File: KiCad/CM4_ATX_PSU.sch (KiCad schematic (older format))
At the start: 2 parts, among them J7 39-28-1243, U2 AP7363-33D

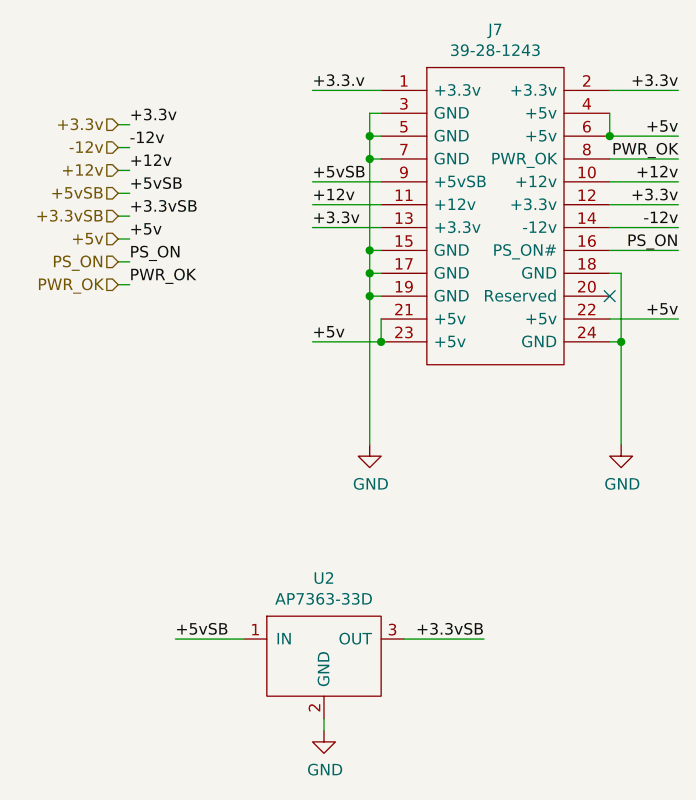
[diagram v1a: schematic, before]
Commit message: Added buffering caps to U2 (3.3vSB provider)
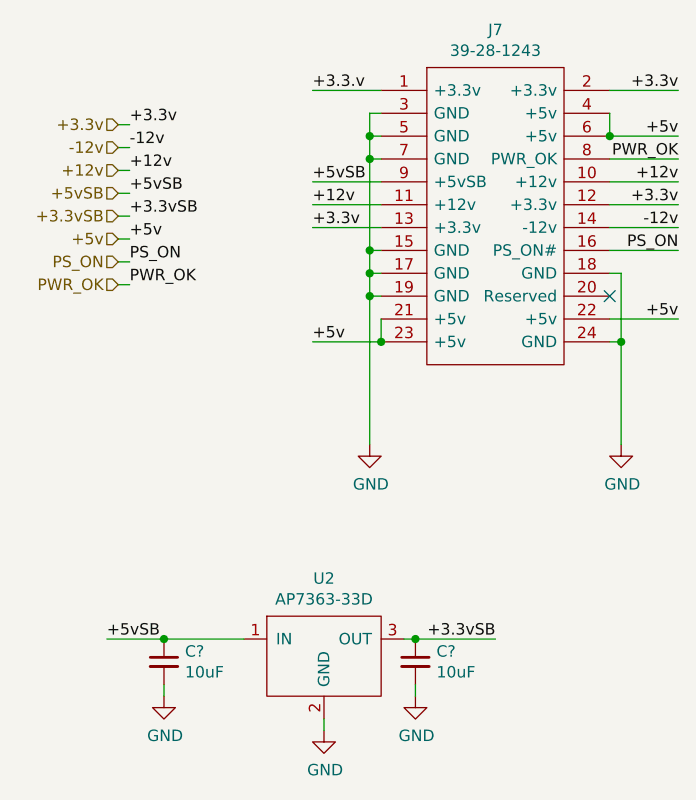
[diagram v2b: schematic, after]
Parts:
- added C? (x2): 10uF, symbol CM4_MATX:C_Small
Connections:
- net +3.3vSB: now also C?.1
- net +5vSB: now also C?.1
- net GND: now also C?.2, C?.2
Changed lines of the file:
@@
 Wire Wire Line
 	4800 4300 4850 4300
-Text Label 5050 5950 0    50   ~ 0
+Text Label 4750 5950 0    50   ~ 0
 +5vSB
 $Comp
@@
 	1    0    0    -1
 $EndComp
-Text Label 6400 5950 2    50   ~ 0
+Text Label 6450 5950 2    50   ~ 0
 +3.3vSB
 Wire Wire Line
-	5050 5950 5350 5950
+	4750 5950 5000 5950
 Wire Wire Line
-	6050 5950 6400 5950
+	6100 5950 6450 5950
 $Comp
 L CM4_MATX:GND #PWR0209
@@
 Wire Wire Line
 	4800 4100 4850 4100
+$Comp
+L CM4_MATX:C_Small C?
+U 1 1 602F3F91
+P 5000 6050
+F 0 "C?" H 5092 6096 50  0000 L CNN
+F 1 "10uF" H 5092 6005 50  0000 L CNN
+F 2 "" H 5000 6050 50  0001 C CNN
+F 3 "~" H 5000 6050 50  0001 C CNN
+	1    5000 6050
+	1    0    0    -1
+$EndComp
+Connection ~ 5000 5950
+Wire Wire Line
+	5000 5950 5350 5950
+$Comp
+L CM4_MATX:GND #PWR?
+U 1 1 602F5A61
+P 5000 6200
+F 0 "#PWR?" H 5000 5950 50  0001 C CNN
+F 1 "GND" H 5005 6027 50  0000 C CNN
+F 2 "" H 5000 6200 50  0001 C CNN
+F 3 "" H 5000 6200 50  0001 C CNN
+	1    5000 6200
+	1    0    0    -1
+$EndComp
+Wire Wire Line
+	5000 6200 5000 6150
+$Comp
+L CM4_MATX:C_Small C?
+U 1 1 602F74E7
+P 6100 6050
+F 0 "C?" H 6192 6096 50  0000 L CNN
+F 1 "10uF" H 6192 6005 50  0000 L CNN
+F 2 "" H 6100 6050 50  0001 C CNN
+F 3 "~" H 6100 6050 50  0001 C CNN
+	1    6100 6050
+	1    0    0    -1
+$EndComp
+Wire Wire Line
+	6100 5950 6050 5950
+Connection ~ 6100 5950
+$Comp
+L CM4_MATX:GND #PWR?
+U 1 1 602F8449
+P 6100 6200
+F 0 "#PWR?" H 6100 5950 50  0001 C CNN
+F 1 "GND" H 6105 6027 50  0000 C CNN
+F 2 "" H 6100 6200 50  0001 C CNN
+F 3 "" H 6100 6200 50  0001 C CNN
+	1    6100 6200
+	1    0    0    -1
+$EndComp
+Wire Wire Line
+	6100 6200 6100 6150
 $EndSCHEMATC

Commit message: Started picking passive components, overhauled library
Cleaned up a bunch of schematic library references.
Added datasheets, descriptions for a lot of existing parts.
Picked most capacitor parts, still a couple left.
Cleaned up a fair few footprint references.
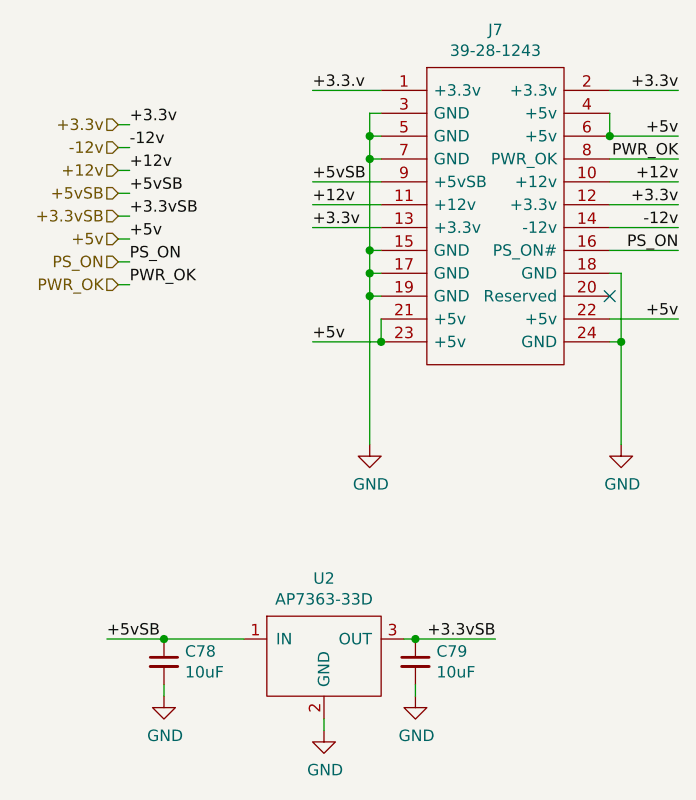
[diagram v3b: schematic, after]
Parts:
- C78, C79: renamed from C?; footprint (none) -> CM4_MATX:C_0603_1608Metric_Pad1.08x0.95mm_HandSolder; Description (none) -> 6.3V 10uF X5R 0603 20% Tol; Mfr. (none) -> Samsung; Mfr. No (none) -> CL10A106MQ8NNNC; Mouser Part Number (none) -> 187-CL10A106MQ8NNNC; Mouser Price/Stock (none) -> https://www.mouser.co.uk/ProductDetail/Samsung-Electro-Mech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
- J7: Height 13.1 -> (none); Manufacturer_Name Molex -> (none); Manufacturer_Part_Number 39-28-1243 -> (none); Mfr. (none) -> Molex; Mfr. No (none) -> 39-28-1243
- U2: footprint (none) -> CM4_MATX:TO-252-3_TabPin2; Description (none) -> LDO Voltage Regulators 1.5A Fast Transient Ultra-LDO Linear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; Mfr. (none) -> Diodes Inc.; Mfr. No (none) -> AP7363-33D-13; Mouser Part Number (none) -> 621-AP7363-33D-13; Mouser Price/Stock (none) -> https://www.mouser.co.uk/ProductDetail/Diodes-Incorporated/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
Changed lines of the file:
@@
 F 1 "39-28-1243" H 6450 3724 50  0000 C CNN
 F 2 "CM4_MATX:SHDR24W125P550X420_2X12_5160X960X1310P" H 6000 4500 50  0001 L CNN
-F 3 "" H 6700 3550 50  0001 L CNN
+F 3 "https://www.mouser.co.uk/datasheet/2/276/0039281243_PCB_HEADERS-228405.pdf" H 6700 3550 50  0001 L CNN
 F 4 "24 way vertical PCB header,Mini-Fit Jr Molex MINI-FIT JR. Series, Series Number 5566, 4.2mm Pitch 24 Way 2 Row Straight PCB Header, Solder Termination, 6A" H 6000 4300 50  0001 L CNN "Description"
-F 5 "13.1" H 6000 4200 50  0001 L CNN "Height"
-F 6 "538-39-28-1243" H 6000 4100 50  0001 L CNN "Mouser Part Number"
-F 7 "https://www.mouser.co.uk/ProductDetail/Molex/39-28-1243?qs=4XSMV6Twtb0I%2F4%252BTTSJFbg%3D%3D" H 6000 4000 50  0001 L CNN "Mouser Price/Stock"
-F 8 "Molex" H 6000 3900 50  0001 L CNN "Manufacturer_Name"
-F 9 "39-28-1243" H 6000 3800 50  0001 L CNN "Manufacturer_Part_Number"
+F 5 "538-39-28-1243" H 6000 4100 50  0001 L CNN "Mouser Part Number"
+F 6 "https://www.mouser.co.uk/ProductDetail/Molex/39-28-1243?qs=4XSMV6Twtb0I%2F4%252BTTSJFbg%3D%3D" H 6000 4000 50  0001 L CNN "Mouser Price/Stock"
+F 7 "Molex" H 5950 3550 50  0001 C CNN "Mfr."
+F 8 "39-28-1243" H 5950 3550 50  0001 C CNN "Mfr. No"
 	1    5950 3550
 	1    0    0    -1
@@
 	5900 3750 5900 3850
 $Comp
-L power:GND #PWR0109
+L CM4_MATX:GND #PWR0109
 U 1 1 601F254C
 P 5900 5100
@@
 	5900 4450 5900 5100
 $Comp
-L power:GND #PWR0110
+L CM4_MATX:GND #PWR0110
 U 1 1 5FF31AD9
 P 7000 5100
@@
 F 0 "U2" H 5700 6215 50  0000 C CNN
 F 1 "AP7363-33D" H 5700 6124 50  0000 C CNN
-F 2 "" H 5700 5950 50  0001 C CNN
+F 2 "CM4_MATX:TO-252-3_TabPin2" H 5700 5950 50  0001 C CNN
 F 3 "https://www.mouser.co.uk/datasheet/2/115/AP7363-247326.pdf" H 5700 5950 50  0001 C CNN
+F 4 "Diodes Inc." H 5700 5950 50  0001 C CNN "Mfr."
+F 5 "AP7363-33D-13" H 5700 5950 50  0001 C CNN "Mfr. No"
+F 6 "621-AP7363-33D-13" H 5700 5950 50  0001 C CNN "Mouser Part Number"
+F 7 "https://www.mouser.co.uk/ProductDetail/Diodes-Incorporated/AP7363-33D-13/?qs=%2Fha2pyFadugx5jr4Zj5yqo2rf4G2BFwG0SXqAhZYbUZbnjJLR6QP1A%3D%3D" H 5700 5950 50  0001 C CNN "Mouser Price/Stock"
+F 8 "LDO Voltage Regulators 1.5A Fast Transient Ultra-LDO Linear Reg" H 5700 5950 50  0001 C CNN "Description"
 	1    5700 5950
 	1    0    0    -1
@@
 	4800 4100 4850 4100
 $Comp
-L CM4_MATX:C_Small C?
+L CM4_MATX:C_Small C78
 U 1 1 602F3F91
 P 5000 6050
-F 0 "C?" H 5092 6096 50  0000 L CNN
+F 0 "C78" H 5092 6096 50  0000 L CNN
 F 1 "10uF" H 5092 6005 50  0000 L CNN
-F 2 "" H 5000 6050 50  0001 C CNN
-F 3 "~" H 5000 6050 50  0001 C CNN
+F 2 "CM4_MATX:C_0603_1608Metric_Pad1.08x0.95mm_HandSolder" H 5000 6050 50  0001 C CNN
+F 3 "https://www.mouser.co.uk/datasheet/2/585/MLCC-1837944.pdf" H 5000 6050 50  0001 C CNN
+F 4 "187-CL10A106MQ8NNNC" H 5000 6050 50  0001 C CNN "Mouser Part Number"
+F 5 "https://www.mouser.co.uk/ProductDetail/Samsung-Electro-Mechanics/CL10A106MQ8NNNC/?qs=349EhDEZ59qlB6a%2FjjeGAg%3D%3D" H 5000 6050 50  0001 C CNN "Mouser Price/Stock"
+F 6 "Samsung" H 5000 6050 50  0001 C CNN "Mfr."
+F 7 "CL10A106MQ8NNNC" H 5000 6050 50  0001 C CNN "Mfr. No"
+F 8 "6.3V 10uF X5R 0603 20% Tol" H 5000 6050 50  0001 C CNN "Description"
 	1    5000 6050
 	1    0    0    -1
@@
 	5000 5950 5350 5950
 $Comp
-L CM4_MATX:GND #PWR?
+L CM4_MATX:GND #PWR01
 U 1 1 602F5A61
 P 5000 6200
-F 0 "#PWR?" H 5000 5950 50  0001 C CNN
+F 0 "#PWR01" H 5000 5950 50  0001 C CNN
 F 1 "GND" H 5005 6027 50  0000 C CNN
 F 2 "" H 5000 6200 50  0001 C CNN
@@
 	5000 6200 5000 6150
 $Comp
-L CM4_MATX:C_Small C?
+L CM4_MATX:C_Small C79
 U 1 1 602F74E7
 P 6100 6050
-F 0 "C?" H 6192 6096 50  0000 L CNN
+F 0 "C79" H 6192 6096 50  0000 L CNN
 F 1 "10uF" H 6192 6005 50  0000 L CNN
-F 2 "" H 6100 6050 50  0001 C CNN
-F 3 "~" H 6100 6050 50  0001 C CNN
+F 2 "CM4_MATX:C_0603_1608Metric_Pad1.08x0.95mm_HandSolder" H 6100 6050 50  0001 C CNN
+F 3 "https://www.mouser.co.uk/datasheet/2/585/MLCC-1837944.pdf" H 6100 6050 50  0001 C CNN
+F 4 "187-CL10A106MQ8NNNC" H 6100 6050 50  0001 C CNN "Mouser Part Number"
+F 5 "https://www.mouser.co.uk/ProductDetail/Samsung-Electro-Mechanics/CL10A106MQ8NNNC/?qs=349EhDEZ59qlB6a%2FjjeGAg%3D%3D" H 6100 6050 50  0001 C CNN "Mouser Price/Stock"
+F 6 "Samsung" H 6100 6050 50  0001 C CNN "Mfr."
+F 7 "CL10A106MQ8NNNC" H 6100 6050 50  0001 C CNN "Mfr. No"
+F 8 "6.3V 10uF X5R 0603 20% Tol" H 6100 6050 50  0001 C CNN "Description"
 	1    6100 6050
 	1    0    0    -1
@@
 Connection ~ 6100 5950
 $Comp
-L CM4_MATX:GND #PWR?
+L CM4_MATX:GND #PWR02
 U 1 1 602F8449
 P 6100 6200
-F 0 "#PWR?" H 6100 5950 50  0001 C CNN
+F 0 "#PWR02" H 6100 5950 50  0001 C CNN
 F 1 "GND" H 6105 6027 50  0000 C CNN
 F 2 "" H 6100 6200 50  0001 C CNN

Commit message: Connected all grounds in the schematic and planes
Planes:
In 1 - Ground
In 2 - 3.3v Zone which excludes the IO and 5v Zone around only the IO
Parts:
- added GND (x5): GND, symbol CM4_MATX:GND
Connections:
- net GND: now also GND.1 (GND), GND.1 (GND), GND.1 (GND), GND.1 (GND), GND.1 (GND)
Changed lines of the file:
@@
 	5900 3750 5900 3850
 $Comp
-L CM4_MATX:GND #PWR0109
+L CM4_MATX:GND GND
 U 1 1 601F254C
 P 5900 5100
-F 0 "#PWR0109" H 5900 4850 50  0001 C CNN
+F 0 "GND" H 5900 4850 50  0001 C CNN
 F 1 "GND" H 5905 4927 50  0000 C CNN
 F 2 "" H 5900 5100 50  0001 C CNN
@@
 	5900 4450 5900 5100
 $Comp
-L CM4_MATX:GND #PWR0110
+L CM4_MATX:GND GND
 U 1 1 5FF31AD9
 P 7000 5100
-F 0 "#PWR0110" H 7000 4850 50  0001 C CNN
+F 0 "GND" H 7000 4850 50  0001 C CNN
 F 1 "GND" H 7005 4927 50  0000 C CNN
 F 2 "" H 7000 5100 50  0001 C CNN
@@
 	6100 5950 6450 5950
 $Comp
-L CM4_MATX:GND #PWR0209
+L CM4_MATX:GND GND
 U 1 1 5FECAD45
 P 5700 6350
-F 0 "#PWR0209" H 5700 6100 50  0001 C CNN
+F 0 "GND" H 5700 6100 50  0001 C CNN
 F 1 "GND" H 5705 6177 50  0000 C CNN
 F 2 "" H 5700 6350 50  0001 C CNN
@@
 	5000 5950 5350 5950
 $Comp
-L CM4_MATX:GND #PWR01
+L CM4_MATX:GND GND
 U 1 1 602F5A61
 P 5000 6200
-F 0 "#PWR01" H 5000 5950 50  0001 C CNN
+F 0 "GND" H 5000 5950 50  0001 C CNN
 F 1 "GND" H 5005 6027 50  0000 C CNN
 F 2 "" H 5000 6200 50  0001 C CNN
@@
 Connection ~ 6100 5950
 $Comp
-L CM4_MATX:GND #PWR02
+L CM4_MATX:GND GND
 U 1 1 602F8449
 P 6100 6200
-F 0 "#PWR02" H 6100 5950 50  0001 C CNN
+F 0 "GND" H 6100 5950 50  0001 C CNN
 F 1 "GND" H 6105 6027 50  0000 C CNN
 F 2 "" H 6100 6200 50  0001 C CNN
